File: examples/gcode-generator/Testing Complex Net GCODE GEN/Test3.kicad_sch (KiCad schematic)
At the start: 10 parts, among them J1 Jack-DC, SW1 SW_Push, U1 Wave Gen, U2 LF356, U3 ESP-M2, U4 LD1117V33

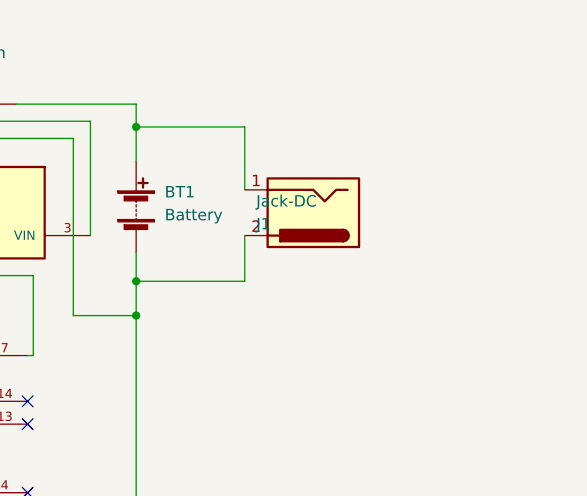
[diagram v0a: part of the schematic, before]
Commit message: Working version with double output layers, needs optimization in printing
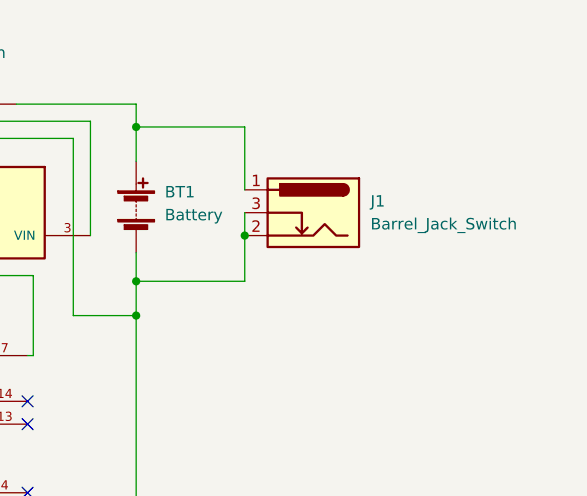
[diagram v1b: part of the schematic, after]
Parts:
- removed J1: Jack-DC, 4DPrinting:charge_port, symbol Connector:Jack-DC
- added J1: Barrel_Jack_Switch, 4DPrinting:charge_port, symbol Connector:Barrel_Jack_Switch
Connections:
- net at BT1.1 (+), SW1.2: now also J1.1
- net at BT1.2 (-), R3.2, U1.1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: now also J1.2, J1.3
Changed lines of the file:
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@@
   (junction (at 184.785 92.71) (diameter 0) (color 0 0 0 0)
+  )
+  (junction (at 196.85 83.82) (diameter 0) (color 0 0 0 0)
   )
   (junction (at 130.175 94.615) (diameter 0) (color 0 0 0 0)
@@
     (stroke (width 0) (type default) (color 0 0 0 0))
   )
+  (wire (pts (xy 196.85 81.28) (xy 196.85 83.82))
+    (stroke (width 0) (type default) (color 0 0 0 0))
+  )
   (wire (pts (xy 196.85 83.82) (xy 196.85 88.9))
     (stroke (width 0) (type default) (color 0 0 0 0))
@@
     (pin "1")
     (pin "2")
+  )
+  (symbol (lib_id "Connector:Barrel_Jack_Switch") (at 204.47 81.28 0) (mirror y) (unit 1)
+    (in_bom yes) (on_board yes) (fields_autoplaced)
+    (property "Reference" "J1" (id 0) (at 210.82 80.0099 0)
+      (effects (font (size 1.27 1.27)) (justify right))
+    )
+    (property "Value" "Barrel_Jack_Switch" (id 1) (at 210.82 82.5499 0)
+      (effects (font (size 1.27 1.27)) (justify right))
+    )
+    (property "Footprint" "4DPrinting:charge_port" (id 2) (at 203.2 82.296 0)
+      (effects (font (size 1.27 1.27)) hide)
+    )
+    (property "Datasheet" "~" (id 3) (at 203.2 82.296 0)
+      (effects (font (size 1.27 1.27)) hide)
+    )
+    (pin "1")
+    (pin "2")
+    (pin "3")
   )
   (symbol (lib_id "power:PWR_FLAG") (at 130.175 76.2 90) (unit 1)
@@
     (pin "2")
   )
-  (symbol (lib_id "Connector:Jack-DC") (at 204.47 81.28 180) (unit 1)
-    (in_bom yes) (on_board yes) (fields_autoplaced)
-    (property "Reference" "J1" (id 0) (at 198.12 82.5501 0)
-      (effects (font (size 1.27 1.27)) (justify right))
-    )
-    (property "Value" "Jack-DC" (id 1) (at 198.12 80.0101 0)
-      (effects (font (size 1.27 1.27)) (justify right))
-    )
-    (property "Footprint" "4DPrinting:charge_port" (id 2) (at 205.74 82.296 0)
-      (effects (font (size 1.27 1.27)) hide)
-    )
-    (property "Datasheet" "~" (id 3) (at 205.74 82.296 0)
-      (effects (font (size 1.27 1.27)) hide)
-    )
-    (pin "1")
-    (pin "2")
-  )
   (sheet_instances
     (path "/" (page "1"))
@@
       (reference "BT1") (unit 1) (value "Battery") (footprint "4DPrinting:Battery")
     )
-    (path "/ec0cd66d-bda3-4649-bb86-0213326ed10d"
-      (reference "J1") (unit 1) (value "Jack-DC") (footprint "4DPrinting:charge_port")
+    (path "/17eb8bef-5041-4495-b1f8-5f87980285a3"
+      (reference "J1") (unit 1) (value "Barrel_Jack_Switch") (footprint "4DPrinting:charge_port")
     )
     (path "/653ec710-1cff-4655-aab8-5fa9652a0533"
